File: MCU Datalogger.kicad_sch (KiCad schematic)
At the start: 25 parts, among them U1 24LC1025, U2 24LC1025, U3 DS1337S_, U4 ATMEGA328P-AU, Y1 32.768 KHz, Y2 16 MHz

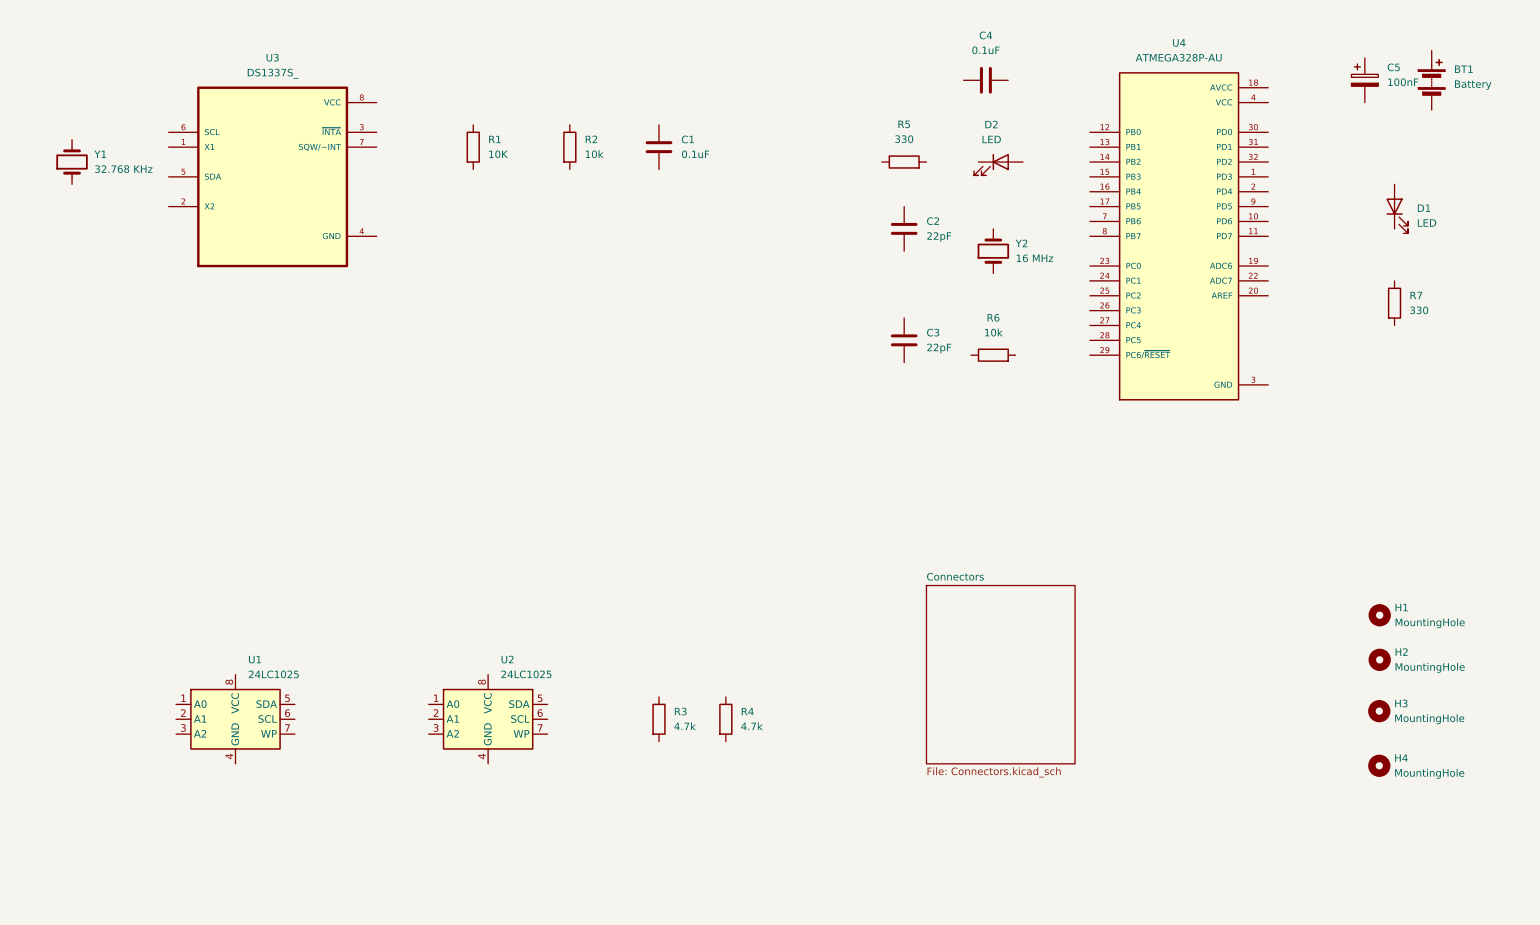
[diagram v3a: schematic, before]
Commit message: completed wiring of main sheet.
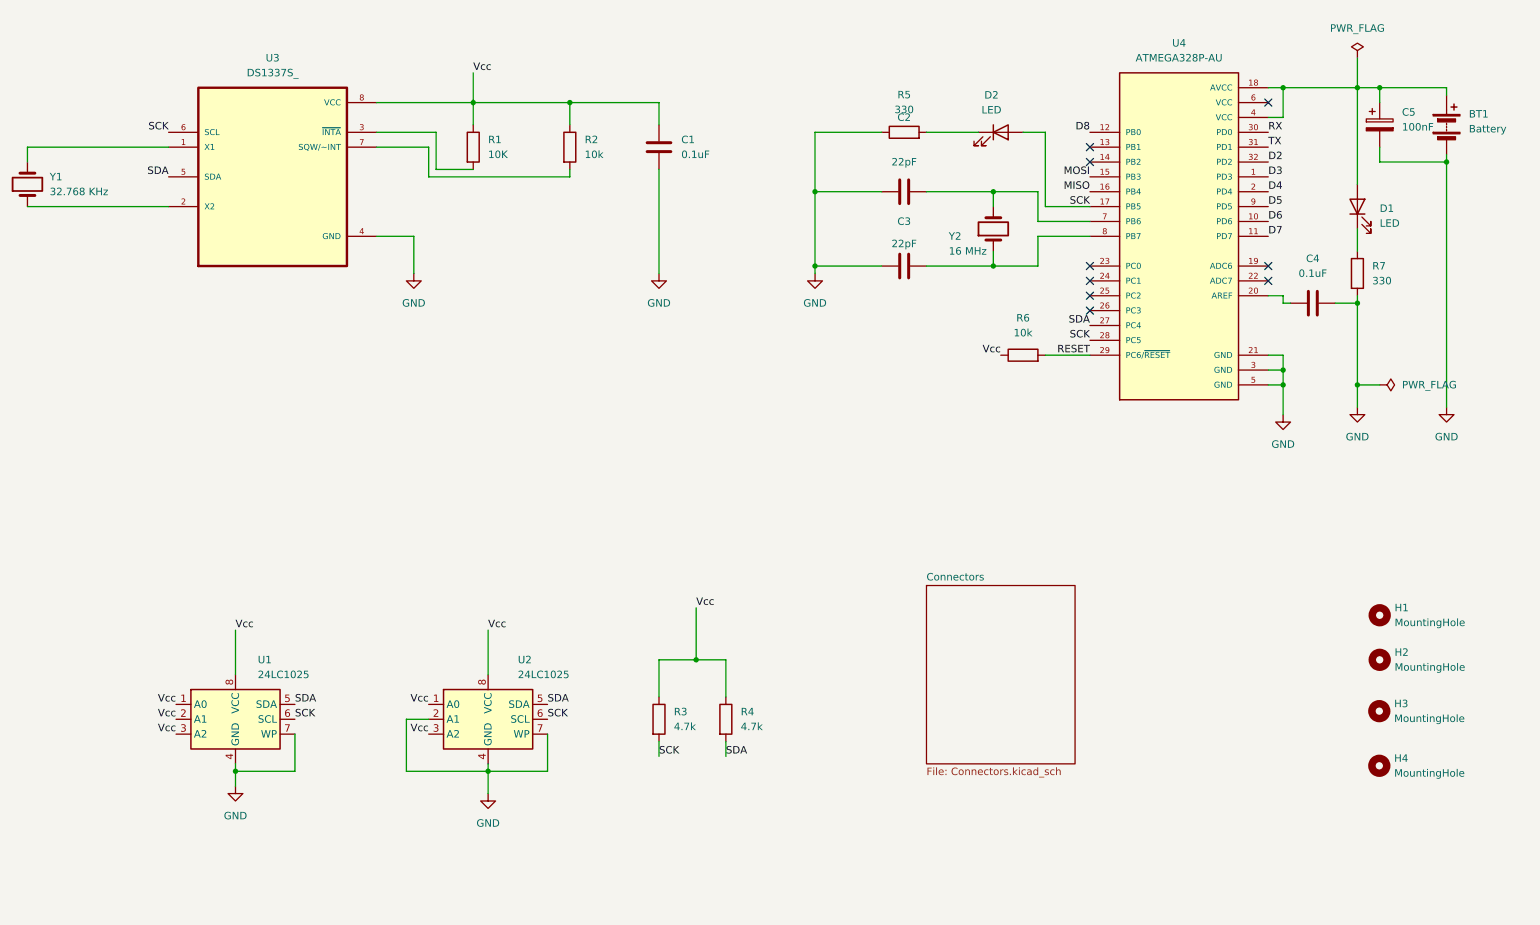
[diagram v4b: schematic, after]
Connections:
- net GND: now also BT1.2 (-), C1.2, C2.1, C3.1, C4.2, C5.2, R5.1, R7.2, U1.4 (GND), U1.7 (WP), U2.2 (A1), U2.4 (GND), U2.7 (WP), U3.4 (GND)
- net at U3.1 (X1): now also Y1.2
- net at U3.2 (X2): now also Y1.1
- net at U3.3 (~{INTA}): now also R1.2
- net SDA: now reaches U3.5 (SDA)
- net SDA: now also R4.2, U1.5 (SDA), U2.5 (SDA), U4.27 (PC4)
- net SCK: now reaches U3.6 (SCL)
- net SCK: now also D2.2 (A), R3.2, U1.6 (SCL), U2.6 (SCL), U4.17 (PB5), U4.28 (PC5)
- net at U3.7 (SQW/~INT): now also R2.2
- net Vcc: now reaches U3.8 (VCC)
- net Vcc: now also C1.1, R1.1, R2.1, R3.1, R4.1, R6.1, U1.1 (A0), U1.2 (A1), U1.3 (A2), U1.8 (VCC), U2.1 (A0), U2.3 (A2), U2.8 (VCC)
- net at C3.2: now also U4.8 (PB7), Y2.1
- net RESET: now reaches R6.2
- net RESET: now also U4.29 (PC6/~{RESET})
- net at D1.1 (K): now also R7.1
- net at D1.2 (A): now also BT1.1 (+), C5.1, U4.18 (AVCC), U4.4 (VCC)
- net at C2.2: now also U4.7 (PB6), Y2.2
- net at C4.1: now also U4.20 (AREF)
- net at D2.1 (K): now also R5.2
- net D3: now reaches U4.1 (PD3)
- net D6: now reaches U4.10 (PD6)
- net D7: now reaches U4.11 (PD7)
- net D8: now reaches U4.12 (PB0)
- net MOSI: now reaches U4.15 (PB3)
- net MISO: now reaches U4.16 (PB4)
- net D4: now reaches U4.2 (PD4)
- net RX: now reaches U4.30 (PD0)
- net TX: now reaches U4.31 (PD1)
- net D2: now reaches U4.32 (PD2)
- net D5: now reaches U4.9 (PD5)
- net VCC: no longer names the net of U4.6 (VCC)
- net VCC: no longer U4.4 (VCC)
- no-connect marks 0 -> 9
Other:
- moved on the sheet: BT1, C2, C3, C4, C5, D1, D2, R5, R6, R7, Y1, Y2

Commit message: completed wiring in the second sheet.
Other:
- sheet Connectors ports: added D2, D3, D4, D5, D6, D7, D8, GND, MISO, MOSI, RESET, RX, SCK, SDA, TX, Vcc; removed none

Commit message: completed commets.
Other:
- note added: "EEPROM"
- note added: "MCU"
- note added: "Mounting"
- note added: "Real time clock"
- moved on the sheet: C1, H1, H2, H3, H4, R1, R2, R3, R4, Y1

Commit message: finshing silkscreen.
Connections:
- net Vcc: now also BT1.1 (+), C5.1, D1.2 (A), U4.18 (AVCC), U4.4 (VCC)
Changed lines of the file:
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@@
+	)
+	(label "Vcc"
+		(at 252.73 39.37 0)
+		(effects
+			(font
+				(size 1.27 1.27)
+			)
+			(justify left bottom)
+		)
 	)
 	(label "Vcc"
@@
 		(dnp no)
 		(property "Reference" "C2"
-			(at 165.1 44.45 90)
-			(effects
-				(font
+			(at 168.91 54.61 90)
+			(effects
+				(font
